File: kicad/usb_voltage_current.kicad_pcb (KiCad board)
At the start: 2 copper layers, 72 x 47 mm, 20 parts, among them J1 Conn_01x01, J10 Conn_01x01, J11 Conn_01x01, J12 Conn_01x01, J13 Conn_01x01, J14 Conn_01x01, J2 Conn_01x01, J3 Conn_01x01, J4 Conn_01x01, J5 Conn_01x01, J6 Conn_01x01, J7 Conn_01x01, J8 Conn_01x01, J9 Conn_01x01, U1 SeeeduinoXIAO, U2 INA226

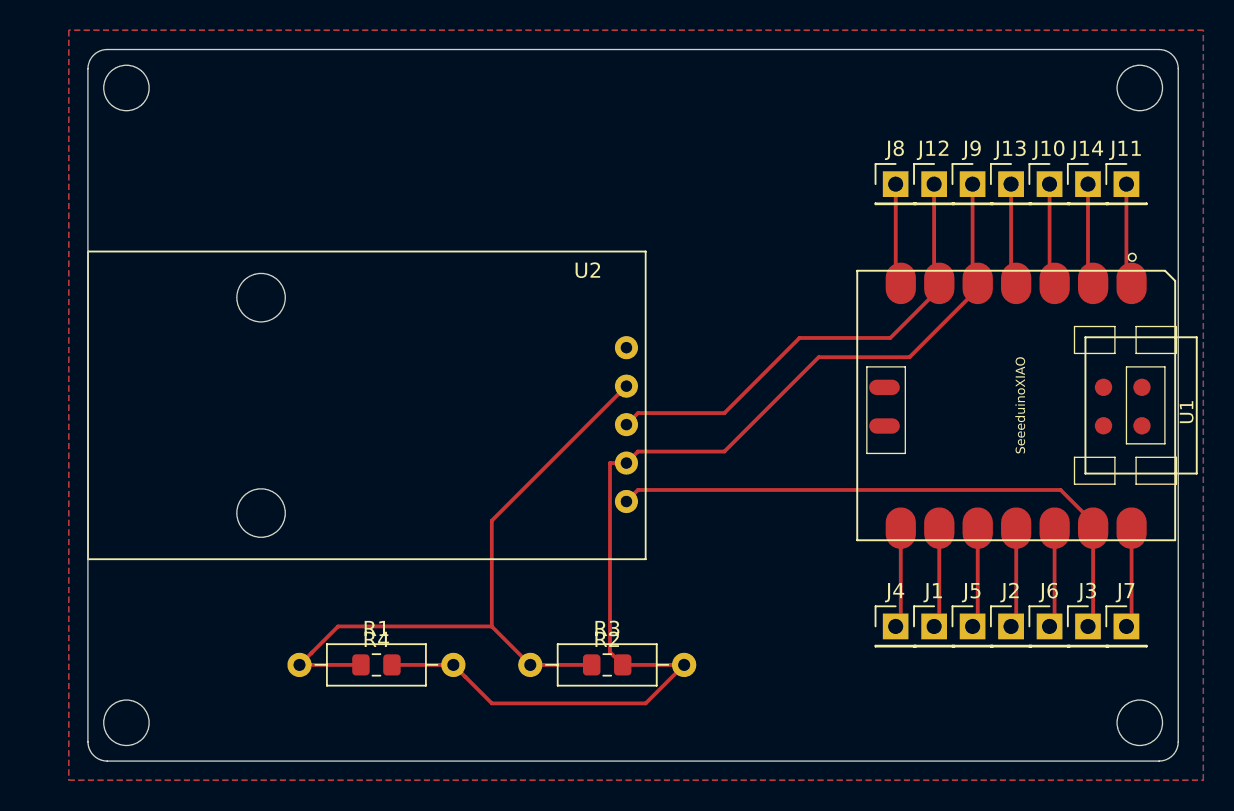
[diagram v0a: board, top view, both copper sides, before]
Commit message: REALGLOBEのシルクを追加
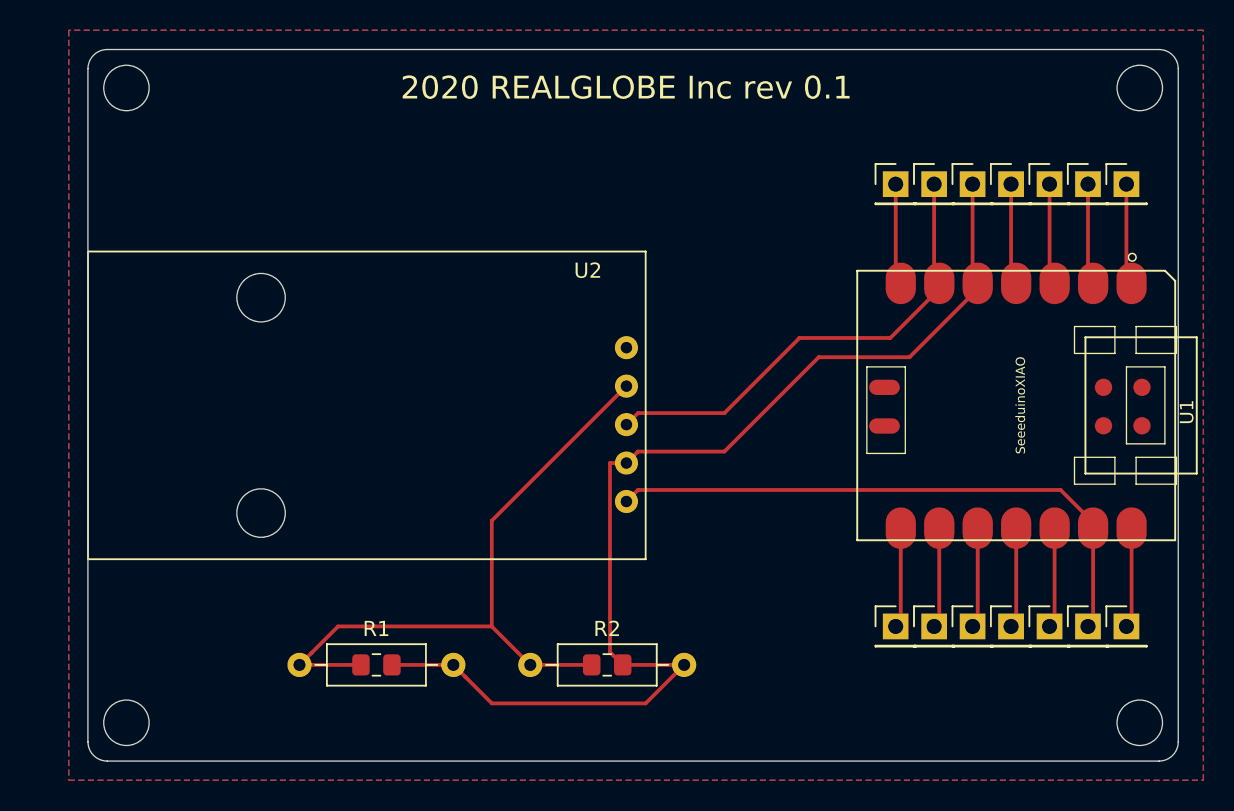
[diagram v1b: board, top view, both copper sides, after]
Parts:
- renumbered R3 to R2, J1 to ~, J10 to ~, J11 to ~, J12 to ~, J13 to ~, J14 to ~, R2 to ~, R4 to ~, J2 to ~, J3 to ~, J4 to ~, J5 to ~, J6 to ~, J7 to ~, J8 to ~, J9 to ~
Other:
- board text added: "2020 REALGLOBE Inc rev 0.1"
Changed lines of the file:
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@@
   (general
     (thickness 1.6)
-    (drawings 12)
+    (drawings 13)
     (tracks 63)
     (zones 0)
@@
   (page A4)
   (layers
-    (0 F.Cu signal)
-    (31 B.Cu signal)
+    (0 F.Cu signal hide)
+    (31 B.Cu signal hide)
     (32 B.Adhes user)
     (33 F.Adhes user)
@@
     (pcbplotparams
       (layerselection 0x010fc_ffffffff)
-      (usegerberextensions false)
+      (usegerberextensions true)
       (usegerberattributes false)
       (usegerberadvancedattributes false)
@@
       (outputformat 1)
       (mirror false)
-      (drillshape 1)
+      (drillshape 0)
       (scaleselection 1)
-      (outputdirectory ""))
+      (outputdirectory "gerbers"))
   )
   (net 0 "")
@@
     (descr "Through hole straight pin header, 1x01, 2.54mm pitch, single row")
     (tags "Through hole pin header THT 1x01 2.54mm single row")
-    (fp_text reference J1 (at 0 -2.33) (layer F.SilkS)
+    (fp_text reference ~ (at 0 -2.33) (layer F.SilkS)
       (effects (font (size 1 1) (thickness 0.15)))
     )
@@
     (descr "Through hole straight pin header, 1x01, 2.54mm pitch, single row")
     (tags "Through hole pin header THT 1x01 2.54mm single row")
-    (fp_text reference J2 (at 0 -2.33) (layer F.SilkS)
+    (fp_text reference ~ (at 0 -2.33) (layer F.SilkS)
       (effects (font (size 1 1) (thickness 0.15)))
     )
@@
     (descr "Through hole straight pin header, 1x01, 2.54mm pitch, single row")
     (tags "Through hole pin header THT 1x01 2.54mm single row")
-    (fp_text reference J3 (at 0 -2.33) (layer F.SilkS)
+    (fp_text reference ~ (at 0 -2.33) (layer F.SilkS)
       (effects (font (size 1 1) (thickness 0.15)))
     )
@@
     (descr "Through hole straight pin header, 1x01, 2.54mm pitch, single row")
     (tags "Through hole pin header THT 1x01 2.54mm single row")
-    (fp_text reference J4 (at 0 -2.33) (layer F.SilkS)
+    (fp_text reference ~ (at 0 -2.33) (layer F.SilkS)
       (effects (font (size 1 1) (thickness 0.15)))
     )
@@
     (descr "Through hole straight pin header, 1x01, 2.54mm pitch, single row")
     (tags "Through hole pin header THT 1x01 2.54mm single row")
-    (fp_text reference J5 (at 0 -2.33) (layer F.SilkS)
+    (fp_text reference ~ (at 0 -2.33) (layer F.SilkS)
       (effects (font (size 1 1) (thickness 0.15)))
     )
@@
     (descr "Through hole straight pin header, 1x01, 2.54mm pitch, single row")
     (tags "Through hole pin header THT 1x01 2.54mm single row")
-    (fp_text reference J6 (at 0 -2.33) (layer F.SilkS)
+    (fp_text reference ~ (at 0 -2.33) (layer F.SilkS)
       (effects (font (size 1 1) (thickness 0.15)))
     )
@@
     (descr "Through hole straight pin header, 1x01, 2.54mm pitch, single row")
     (tags "Through hole pin header THT 1x01 2.54mm single row")
-    (fp_text reference J7 (at 0 -2.33) (layer F.SilkS)
+    (fp_text reference ~ (at 0 -2.33) (layer F.SilkS)
       (effects (font (size 1 1) (thickness 0.15)))
     )
@@
     (descr "Through hole straight pin header, 1x01, 2.54mm pitch, single row")
     (tags "Through hole pin header THT 1x01 2.54mm single row")
-    (fp_text reference J8 (at 0 -2.33) (layer F.SilkS)
+    (fp_text reference ~ (at 0 -2.33) (layer F.SilkS)
       (effects (font (size 1 1) (thickness 0.15)))
     )
@@
     (descr "Through hole straight pin header, 1x01, 2.54mm pitch, single row")
     (tags "Through hole pin header THT 1x01 2.54mm single row")
-    (fp_text reference J9 (at 0 -2.33) (layer F.SilkS)
+    (fp_text reference ~ (at 0 -2.33) (layer F.SilkS)
       (effects (font (size 1 1) (thickness 0.15)))
     )
@@
     (descr "Through hole straight pin header, 1x01, 2.54mm pitch, single row")
     (tags "Through hole pin header THT 1x01 2.54mm single row")
-    (fp_text reference J10 (at 0 -2.33) (layer F.SilkS)
+    (fp_text reference ~ (at 0 -2.33) (layer F.SilkS)
       (effects (font (size 1 1) (thickness 0.15)))
     )
@@
     (descr "Through hole straight pin header, 1x01, 2.54mm pitch, single row")
     (tags "Through hole pin header THT 1x01 2.54mm single row")
-    (fp_text reference J11 (at 0 -2.33) (layer F.SilkS)
+    (fp_text reference ~ (at 0 -2.33) (layer F.SilkS)
       (effects (font (size 1 1) (thickness 0.15)))
     )
@@
     (descr "Through hole straight pin header, 1x01, 2.54mm pitch, single row")
     (tags "Through hole pin header THT 1x01 2.54mm single row")
-    (fp_text reference J12 (at 0 -2.33) (layer F.SilkS)
+    (fp_text reference ~ (at 0 -2.33) (layer F.SilkS)
       (effects (font (size 1 1) (thickness 0.15)))
     )
@@
     (descr "Through hole straight pin header, 1x01, 2.54mm pitch, single row")
     (tags "Through hole pin header THT 1x01 2.54mm single row")
-    (fp_text reference J13 (at 0 -2.33) (layer F.SilkS)
+    (fp_text reference ~ (at 0 -2.33) (layer F.SilkS)
       (effects (font (size 1 1) (thickness 0.15)))
     )
@@
     (descr "Through hole straight pin header, 1x01, 2.54mm pitch, single row")
     (tags "Through hole pin header THT 1x01 2.54mm single row")
-    (fp_text reference J14 (at 0 -2.33) (layer F.SilkS)
+    (fp_text reference ~ (at 0 -2.33) (layer F.SilkS)
       (effects (font (size 1 1) (thickness 0.15)))
     )
@@
     (tags "resistor handsolder")
     (attr smd)
-    (fp_text reference R2 (at 0 -1.65) (layer F.SilkS)
+    (fp_text reference ~ (at 0 -1.65) (layer F.SilkS)
       (effects (font (size 1 1) (thickness 0.15)))
     )
@@
     (descr "Resistor, Axial_DIN0207 series, Axial, Horizontal, pin pitch=10.16mm, 0.25W = 1/4W, length*diameter=6.3*2.5mm^2, http://cdn-reichelt.de/documents/datenblatt/B400/1_4W%23YAG.pdf")
     (tags "Resistor Axial_DIN0207 series Axial Horizontal pin pitch 10.16mm 0.25W = 1/4W length 6.3mm diameter 2.5mm")
-    (fp_text reference R3 (at 5.08 -2.37) (layer F.SilkS)
+    (fp_text reference R2 (at 5.08 -2.37) (layer F.SilkS)
       (effects (font (size 1 1) (thickness 0.15)))
     )
@@
     (tags "resistor handsolder")
     (attr smd)
-    (fp_text reference R4 (at 0 -1.65) (layer F.SilkS)
+    (fp_text reference ~ (at 0 -1.65) (layer F.SilkS)
       (effects (font (size 1 1) (thickness 0.15)))
     )
@@
     (pad "" np_thru_hole circle (at 11.43 -17.272) (size 3.2 3.2) (drill 3.2) (layers *.Cu *.Mask))
   )
+  (gr_text "2020 REALGLOBE Inc rev 0.1" (at 72.39 39.37) (layer F.SilkS)
+    (effects (font (size 1.5 1.5) (thickness 0.3)))
+  )
   (gr_arc (start 107.56 38.1) (end 108.83 38.1) (angle -90) (layer Edge.Cuts) (width 0.05))

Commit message: AW修正
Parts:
- moved R2 15.2 mm to (55.9, 77.5)
- moved R4 15.2 mm to (71.1, 77.5)
- renumbered ~ to J1, ~ to J10, ~ to J11, ~ to J12, ~ to J13, ~ to J14, ~ to J2, ~ to J3, ~ to J4, ~ to J5, ~ to J6, ~ to J7, ~ to J8, ~ to J9, ~ to R2, R2 to R3, ~ to R4
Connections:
- J6 pad 1: Net-(J6-Pad1) -> +3V3
- R3 pad 2: Net-(J9-Pad1) -> Net-(J12-Pad1)
- R4 pad 2: Net-(J9-Pad1) -> Net-(J12-Pad1)
- U1 pad 12: Net-(J6-Pad1) -> +3V3
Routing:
- net +3V3: track 45.0 -> 93.6 mm
- net GND: track 39.0 -> 7.01 mm
- net Net-(J12-Pad1): track 31.4 -> 59.6 mm
- net Net-(J6-Pad1): track 6.63 -> 0.00 mm
- net Net-(J9-Pad1): track 75.2 -> 72.5 mm

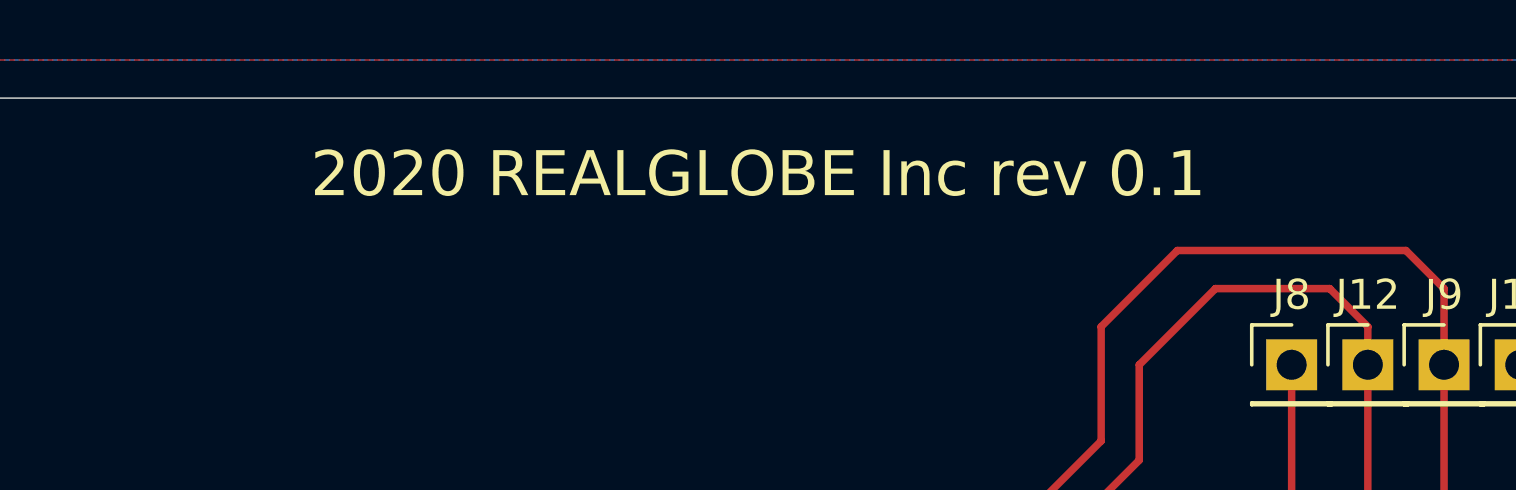
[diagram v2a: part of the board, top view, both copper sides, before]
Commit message: 基板シルクのリビジョンアップ
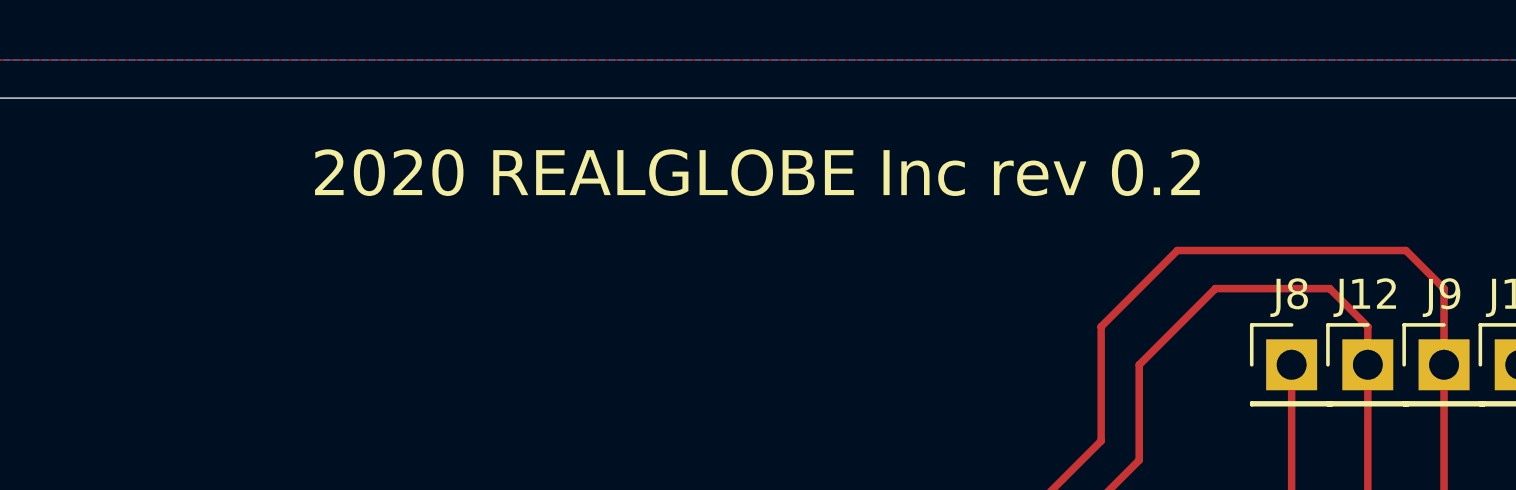
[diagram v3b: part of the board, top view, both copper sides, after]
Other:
- board text added: "2020 REALGLOBE Inc rev 0.2"
- board text removed: "2020 REALGLOBE Inc rev 0.1"
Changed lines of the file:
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@@
       (net 20 "Net-(U1-Pad20)"))
   )
-  (gr_text "2020 REALGLOBE Inc rev 0.1" (at 72.39 39.37) (layer F.SilkS)
+  (gr_text "2020 REALGLOBE Inc rev 0.2" (at 72.39 39.37) (layer F.SilkS)
     (effects (font (size 1.5 1.5) (thickness 0.3)))
   )
